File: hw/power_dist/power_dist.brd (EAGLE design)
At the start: 80 x 50 mm, 69 parts, among them J1 JST-ZH6SMT_VERT, J2 JST-PH4SMT_VERT, J3 JST-PH5VERT, P1 XT30P, P2 XT30P, P3 XT30P, P4 XT30P, P5 XT30P, P6 XT30P, P7 XT90PW-M, Q1 PSMN4R8-100BSEJ, Q2 PSMN4R8-100BSEJ, Q3 PSMN4R8-100BSEJ, Q4 MF-DSC-SOT233-BSS138, Q5 MF-DSC-SOT233-MMBT3906, Q6 MF-DSC-SOT233-MMBT3904, U1 MAX15062AATA+T, U2 STM32G474CEU6, U3 LM5066IPMHE/NOPB, U4 TCAN334G

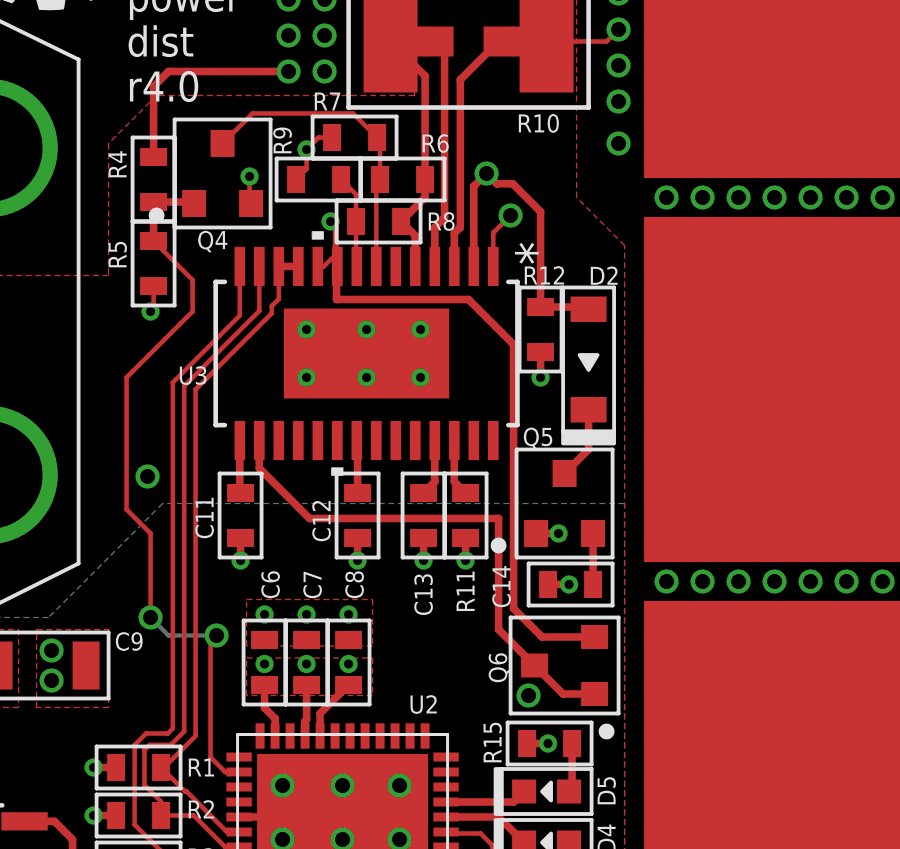
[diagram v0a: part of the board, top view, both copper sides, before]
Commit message: power_dist r4: Add some DNP resistors for PGD and FB
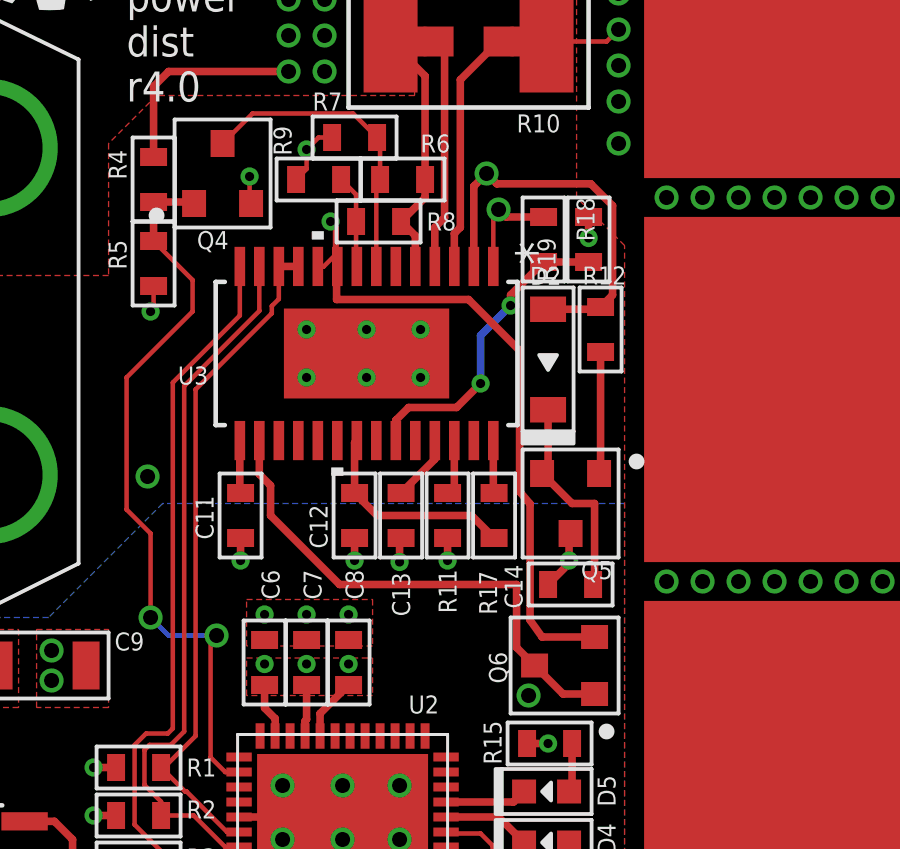
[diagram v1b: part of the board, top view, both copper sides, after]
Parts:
- added R17, R18, R19: DNP, mfpassives:R0603
- moved R12 2.00 mm to (43.8, 32.2)
- moved D2 1.35 mm to (42.0, 31.2)
- moved C13 0.75 mm to (37.1, 26.0)
- moved R11 0.60 mm to (38.7, 26.0)
- moved Q5 0.20 mm to (42.8, 26.4), turned to 270 degrees
- moved C12 0.10 mm to (35.6, 26.0)
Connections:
- removed net PGD: U3.28
- new net N$16: Q5.P$1, R12.P$2
- new net VDD: C12.P$1, R17.P$1, U3.21
- net GND: now also Q5.P$3, R19.P$2; no longer Q5.P$1, R12.P$2
- net N$12: now also R17.P$2, U3.28; no longer C14.P$1, Q5.P$2
- net N$13: now also C14.P$1, Q5.P$2; no longer Q5.P$3
- net N$6: now also R18.P$2, R19.P$1, U3.23; no longer C12.P$1, U3.21
- net VSWITCHED: now also R18.P$1
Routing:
- net N$6: track 1.76 -> 10.4 mm, vias 0 -> 2
- net VDD: track 0.00 -> 7.05 mm
- net N$13: track 2.46 -> 7.09 mm
- net N$16: track 0.00 -> 4.07 mm
- net N$5: track 81.1 -> 84.0 mm
- net VSWITCHED: track 35.7 -> 37.5 mm
- net GND: track 65.5 -> 65.9 mm, vias 61 -> 60
